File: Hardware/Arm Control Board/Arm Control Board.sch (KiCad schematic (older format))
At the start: 31 parts, among them P1 Servo 1, P10 UIM240XX_Stepper_Conn, P11 Battery, P12 SyRen, P13 Raspberry Pi, P2 Shoulder Feedback, P3 Servo 2, P4 Servo 3, P5 Elbow Feedback, P6 Servo 4, P7 RS485, P8 ST_SWD_Connector, P9 Servo 5, U1 STM32F401RCT6, U2 SN75176BDR, U3 74LVCH244APW, X1 24MHz

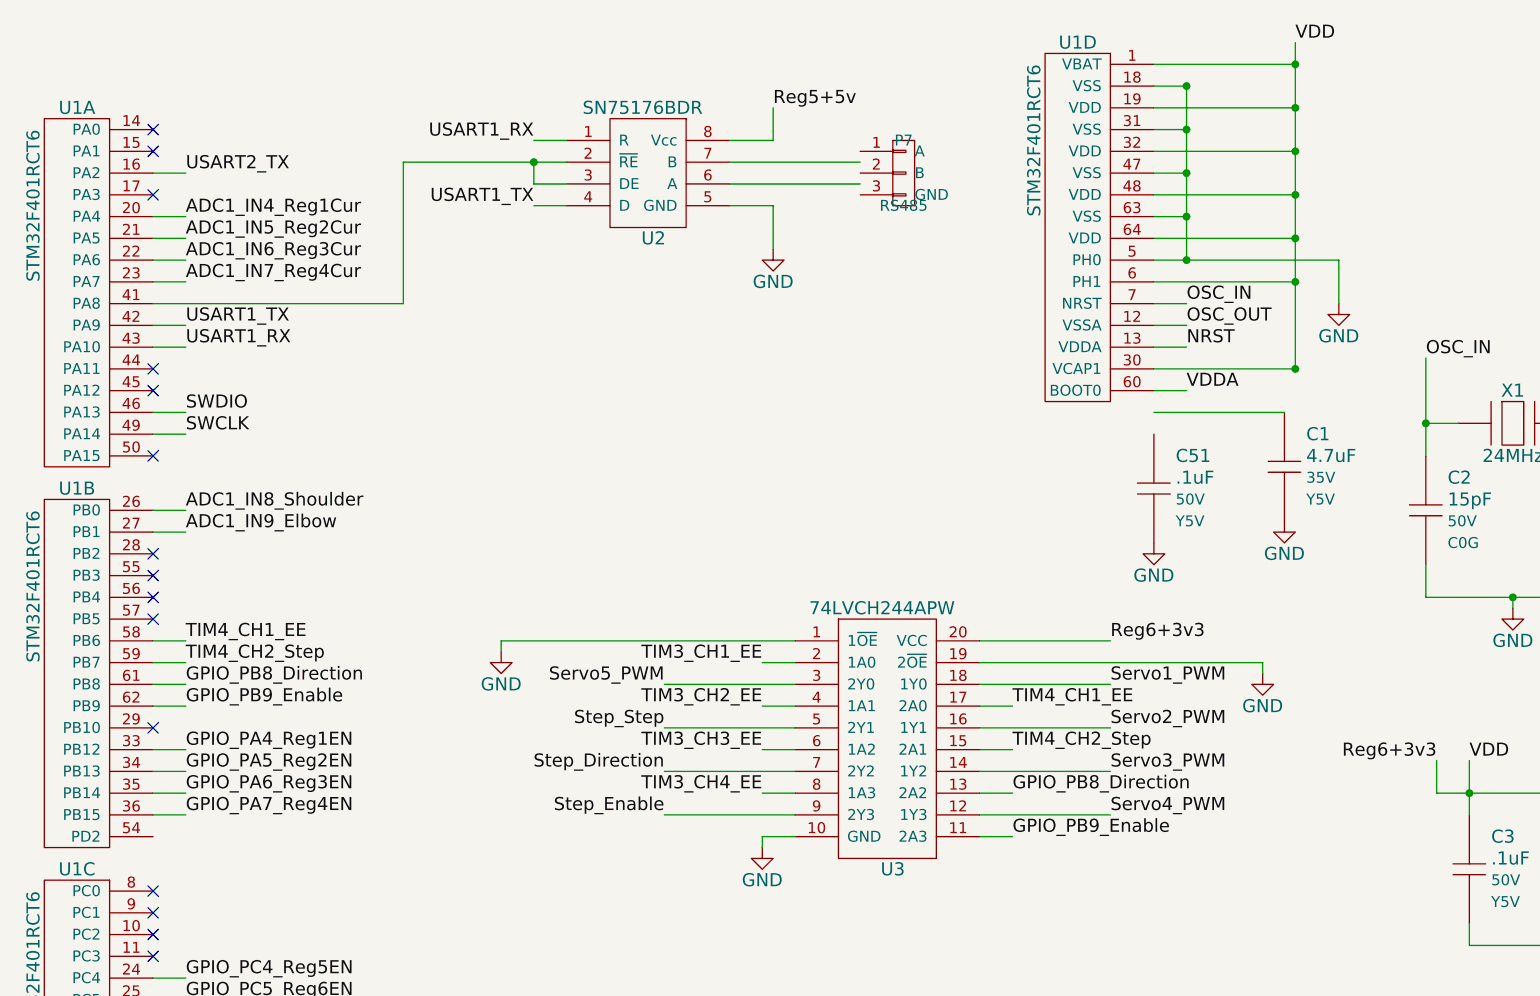
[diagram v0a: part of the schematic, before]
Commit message: Fixed power connections to STM32
The part changes screwed some connections up
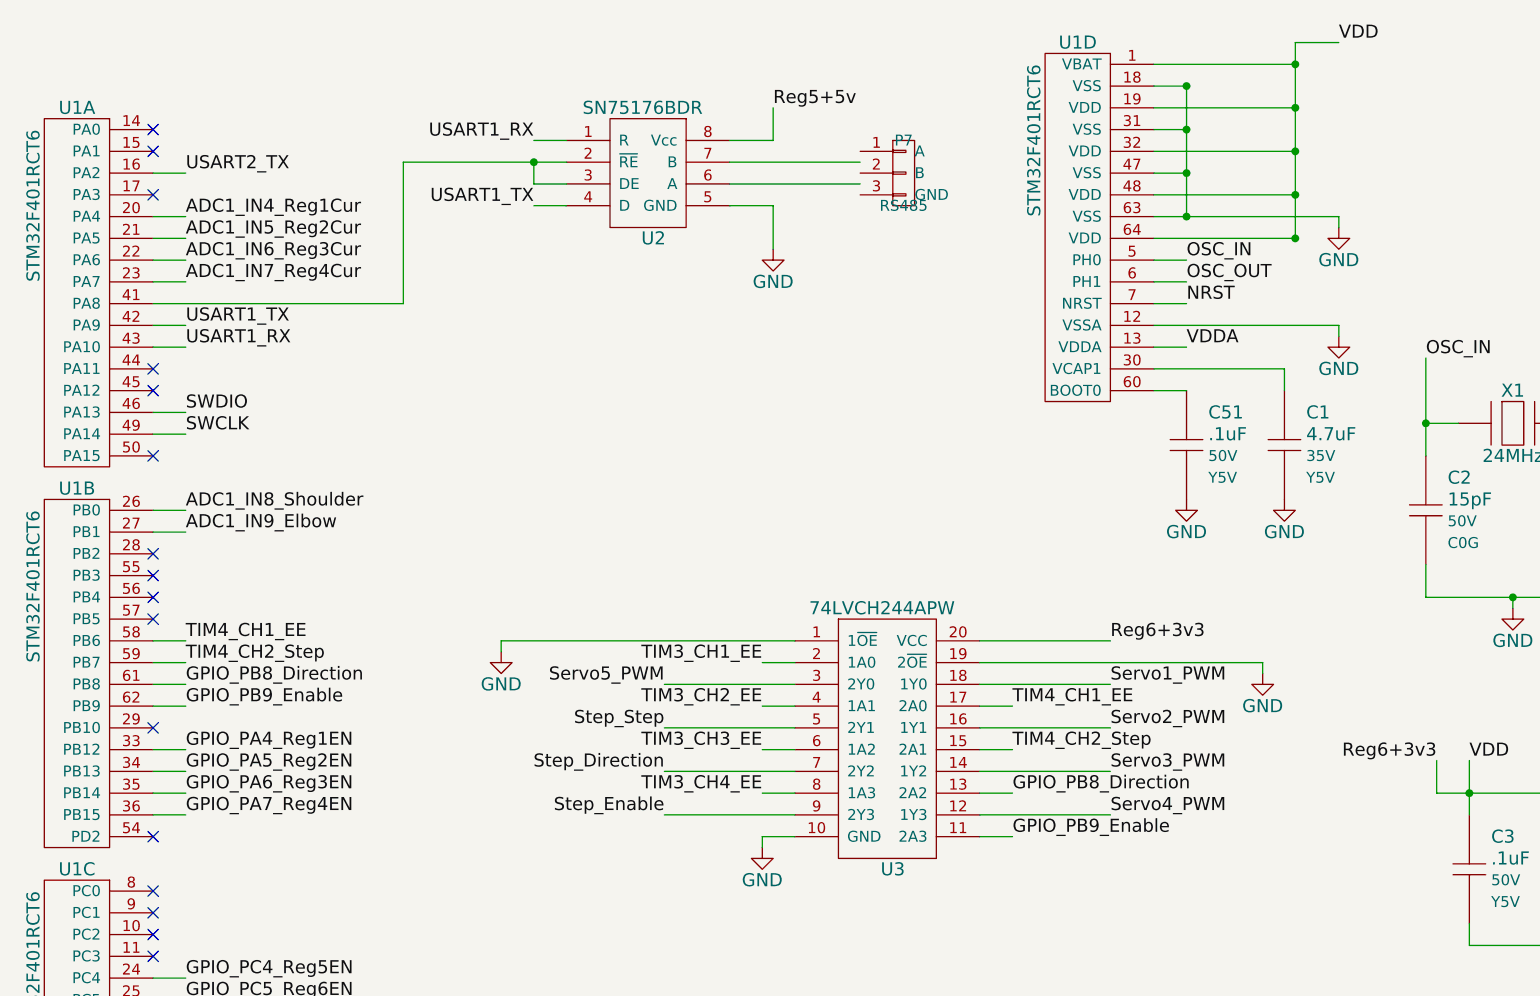
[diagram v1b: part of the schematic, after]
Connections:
- net GND: now also U1.12 (VSSA); no longer U1.5 (PH0)
- net NRST: now also U1.7 (NRST); no longer U1.13 (VDDA)
- net OSC_IN: now also U1.5 (PH0); no longer U1.7 (NRST)
- net OSC_OUT: now also U1.6 (PH1); no longer U1.12 (VSSA)
- net Reg6+3v3: no longer U1.30 (VCAP1), U1.6 (PH1)
- net VDDA: now also U1.13 (VDDA); no longer U1.60 (BOOT0)
- net at C51.1: now also U1.60 (BOOT0)
- net at C1.1: now also U1.30 (VCAP1)
- no-connect marks 22 -> 23
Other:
- moved on the sheet: C1, C51
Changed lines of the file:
@@
 	1    0    0    -1
 $EndComp
-Text Label 6450 650  0    60   ~ 0
+Text Label 6650 650  0    60   ~ 0
 VDD
 $Comp
@@
 Text Label 7250 3950 0    60   ~ 0
 VDD
-Text Label 5950 2250 0    60   ~ 0
+Text Label 5950 2050 0    60   ~ 0
 VDDA
 Text Label 10150 4000 0    60   ~ 0
@@
 Text Label 1350 2450 0    60   ~ 0
 SWCLK
-Text Label 5950 2050 0    60   ~ 0
+Text Label 5950 1850 0    60   ~ 0
 NRST
 $Comp
@@
 L Capacitor C1
 U 1 1 54D0C267
-P 6400 2600
-F 0 "C1" V 6250 2700 60  0000 L CNN
-F 1 "4.7uF" V 6350 2700 60  0000 L CNN
-F 2 "Capacitors_SMD:C_1206_HandSoldering" H 6300 2600 60  0001 C CNN
-F 3 "" H 6400 2700 60  0001 C CNN
-F 4 "Taiyo Yuden" H 6400 2600 60  0001 C CNN "Manufacturer"
-F 5 "GMK316F475ZG-T" H 6400 2600 60  0001 C CNN "Manufacturer Part #"
-F 6 "Digi-Key" H 6400 2600 60  0001 C CNN "Vendor"
-F 7 "587-2254-1-ND" H 6400 2600 60  0001 C CNN "Vendor Part #"
-F 8 "35V" V 6450 2700 50  0000 L CNN "Voltage"
-F 9 "Y5V" V 6550 2700 50  0000 L CNN "Dielectric"
-	1    6400 2600
+P 6400 2500
+F 0 "C1" V 6250 2600 60  0000 L CNN
+F 1 "4.7uF" V 6350 2600 60  0000 L CNN
+F 2 "Capacitors_SMD:C_1206_HandSoldering" H 6300 2500 60  0001 C CNN
+F 3 "" H 6400 2600 60  0001 C CNN
+F 4 "Taiyo Yuden" H 6400 2500 60  0001 C CNN "Manufacturer"
+F 5 "GMK316F475ZG-T" H 6400 2500 60  0001 C CNN "Manufacturer Part #"
+F 6 "Digi-Key" H 6400 2500 60  0001 C CNN "Vendor"
+F 7 "587-2254-1-ND" H 6400 2500 60  0001 C CNN "Vendor Part #"
+F 8 "35V" V 6450 2600 50  0000 L CNN "Voltage"
+F 9 "Y5V" V 6550 2600 50  0000 L CNN "Dielectric"
+	1    6400 2500
 	0    1    1    0
 $EndComp
@@
 L GND #PWR020
 U 1 1 54D0EC2B
-P 6400 2850
-F 0 "#PWR020" H 6400 2600 60  0001 C CNN
-F 1 "GND" H 6400 2700 60  0000 C CNN
-F 2 "" H 6400 2850 60  0000 C CNN
-F 3 "" H 6400 2850 60  0000 C CNN
-	1    6400 2850
-	1    0    0    -1
-$EndComp
-Text Label 5950 1850 0    60   ~ 0
+P 6400 2750
+F 0 "#PWR020" H 6400 2500 60  0001 C CNN
+F 1 "GND" H 6400 2600 60  0000 C CNN
+F 2 "" H 6400 2750 60  0000 C CNN
+F 3 "" H 6400 2750 60  0000 C CNN
+	1    6400 2750
+	1    0    0    -1
+$EndComp
+Text Label 5950 1650 0    60   ~ 0
 OSC_IN
-Text Label 5950 1950 0    60   ~ 0
+Text Label 5950 1750 0    60   ~ 0
 OSC_OUT
 $Comp
@@
 L GND #PWR024
 U 1 1 54CB9E3A
-P 6650 1850
-F 0 "#PWR024" H 6650 1600 60  0001 C CNN
-F 1 "GND" H 6650 1700 60  0000 C CNN
-F 2 "" H 6650 1850 60  0000 C CNN
-F 3 "" H 6650 1850 60  0000 C CNN
-	1    6650 1850
+P 6650 1500
+F 0 "#PWR024" H 6650 1250 60  0001 C CNN
+F 1 "GND" H 6650 1350 60  0000 C CNN
+F 2 "" H 6650 1500 60  0000 C CNN
+F 3 "" H 6650 1500 60  0000 C CNN
+	1    6650 1500
 	1    0    0    -1
 $EndComp
@@
 Wire Wire Line
 	6450 950  5800 950
-Wire Wire Line
-	6450 1750 5800 1750
-Connection ~ 6450 1750
 Wire Wire Line
 	6450 1550 5800 1550
@@
 Wire Wire Line
 	5950 1050 5800 1050
-Wire Wire Line
-	5800 1650 6650 1650
 Connection ~ 5950 1050
 Wire Wire Line
-	5950 1450 5800 1450
+	5800 1450 6650 1450
 Connection ~ 5950 1450
 Wire Wire Line
@@
 Connection ~ 9250 4100
 Wire Wire Line
-	6450 2150 5800 2150
-Connection ~ 6450 2150
-Wire Wire Line
 	9650 4800 9650 4700
 Connection ~ 9650 4800
 Wire Wire Line
-	5800 2250 5950 2250
+	5800 2050 5950 2050
 Wire Wire Line
 	5800 850  5950 850
@@
 	1200 2450 1350 2450
 Wire Wire Line
-	5800 2050 5950 2050
+	5800 1850 5950 1850
 Wire Wire Line
 	5350 6000 5200 6000
@@
 	4050 1100 3850 1100
 Wire Wire Line
-	5800 2350 6400 2350
-Wire Wire Line
-	5800 1850 5950 1850
-Wire Wire Line
-	5800 1950 5950 1950
+	5800 1650 5950 1650
+Wire Wire Line
+	5800 1750 5950 1750
 Wire Wire Line
 	7050 2100 7050 2550
@@
 Connection ~ 8050 5850
 Wire Wire Line
-	5950 850  5950 1650
-Wire Wire Line
-	6650 1650 6650 1850
-Wire Wire Line
-	6450 650  6450 2150
+	6650 1450 6650 1500
 Connection ~ 6450 950
-Connection ~ 5950 1650
 Wire Wire Line
 	5800 750  6450 750
@@
 L Capacitor C51
 U 1 1 54CC6722
-P 5800 2700
-F 0 "C51" V 5650 2800 60  0000 L CNN
-F 1 ".1uF" V 5750 2800 60  0000 L CNN
-F 2 "Capacitors_SMD:C_1206_HandSoldering" H 5700 2700 60  0001 C CNN
-F 3 "" H 5800 2800 60  0001 C CNN
-F 4 "Samsung Electro-Mechanics" H 5800 2700 60  0001 C CNN "Manufacturer"
-F 5 "CL31F104MBCNNNC" H 5800 2700 60  0001 C CNN "Manufacturer Part #"
-F 6 "Digi-Key" H 5800 2700 60  0001 C CNN "Vendor"
-F 7 "1276-2854-1-ND" H 5800 2700 60  0001 C CNN "Vendor Part #"
-F 8 "50V" V 5850 2800 50  0000 L CNN "Voltage"
-F 9 "Y5V" V 5950 2800 50  0000 L CNN "Dielectric"
-	1    5800 2700
+P 5950 2500
+F 0 "C51" V 5800 2600 60  0000 L CNN
+F 1 ".1uF" V 5900 2600 60  0000 L CNN
+F 2 "Capacitors_SMD:C_1206_HandSoldering" H 5850 2500 60  0001 C CNN
+F 3 "" H 5950 2600 60  0001 C CNN
+F 4 "Samsung Electro-Mechanics" H 5950 2500 60  0001 C CNN "Manufacturer"
+F 5 "CL31F104MBCNNNC" H 5950 2500 60  0001 C CNN "Manufacturer Part #"
+F 6 "Digi-Key" H 5950 2500 60  0001 C CNN "Vendor"
+F 7 "1276-2854-1-ND" H 5950 2500 60  0001 C CNN "Vendor Part #"
+F 8 "50V" V 6000 2600 50  0000 L CNN "Voltage"
+F 9 "Y5V" V 6100 2600 50  0000 L CNN "Dielectric"
+	1    5950 2500
 	0    1    1    0
 $EndComp
@@
 L GND #PWR025
 U 1 1 54CC691C
-P 5800 2950
-F 0 "#PWR025" H 5800 2700 60  0001 C CNN
-F 1 "GND" H 5800 2800 60  0000 C CNN
-F 2 "" H 5800 2950 60  0000 C CNN
-F 3 "" H 5800 2950 60  0000 C CNN
-	1    5800 2950
+P 5950 2750
+F 0 "#PWR025" H 5950 2500 60  0001 C CNN
+F 1 "GND" H 5950 2600 60  0000 C CNN
+F 2 "" H 5950 2750 60  0000 C CNN
+F 3 "" H 5950 2750 60  0000 C CNN
+	1    5950 2750
 	1    0    0    -1
 $EndComp
@@
 Text Label 9300 2050 2    60   ~ 0
 ADC1_IN7_Reg4Cur
+NoConn ~ 1200 4300
+Wire Wire Line
+	5950 850  5950 1450
+Wire Wire Line
+	6450 650  6450 1550
+Wire Wire Line
+	5800 2250 5950 2250
+Wire Wire Line
+	5800 2150 6400 2150
+Wire Wire Line
+	6400 2150 6400 2250
+Wire Wire Line
+	6450 650  6650 650
+Wire Wire Line
+	5800 1950 6650 1950
+Wire Wire Line
+	6650 1950 6650 2000
+$Comp
+L GND #PWR?
+U 1 1 54D8F98A
+P 6650 2000
+F 0 "#PWR?" H 6650 1750 60  0001 C CNN
+F 1 "GND" H 6650 1850 60  0000 C CNN
+F 2 "" H 6650 2000 60  0000 C CNN
+F 3 "" H 6650 2000 60  0000 C CNN
+	1    6650 2000
+	1    0    0    -1
+$EndComp
 $EndSCHEMATC

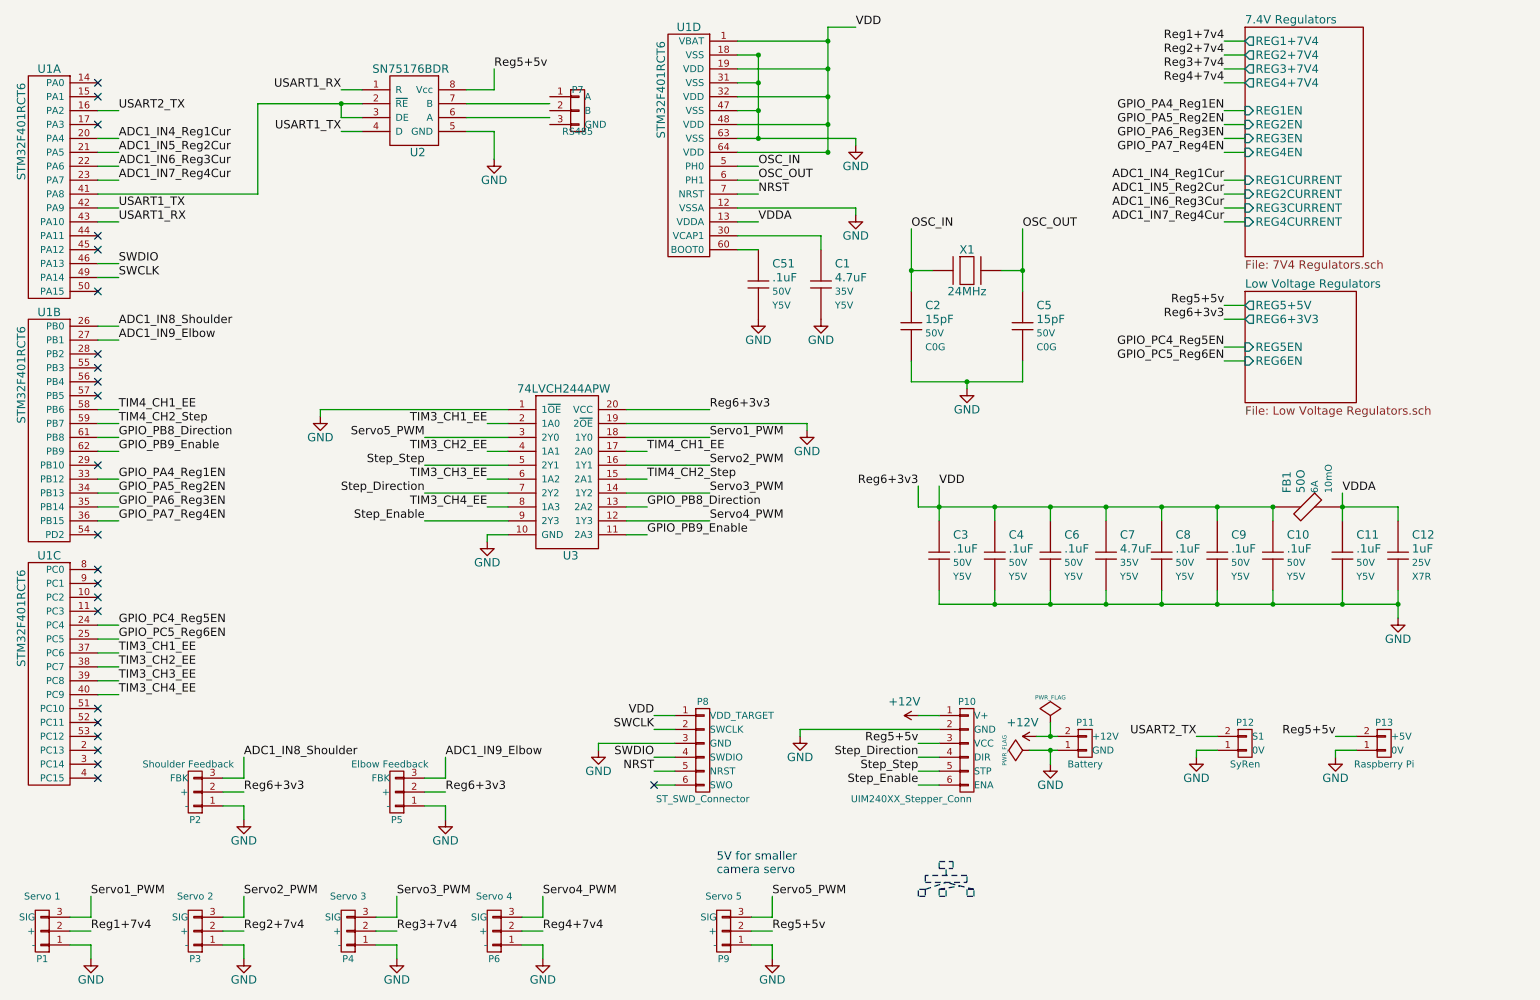
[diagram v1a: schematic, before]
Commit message: Added clamp force sensor port in cube and schematic
Resolves #20
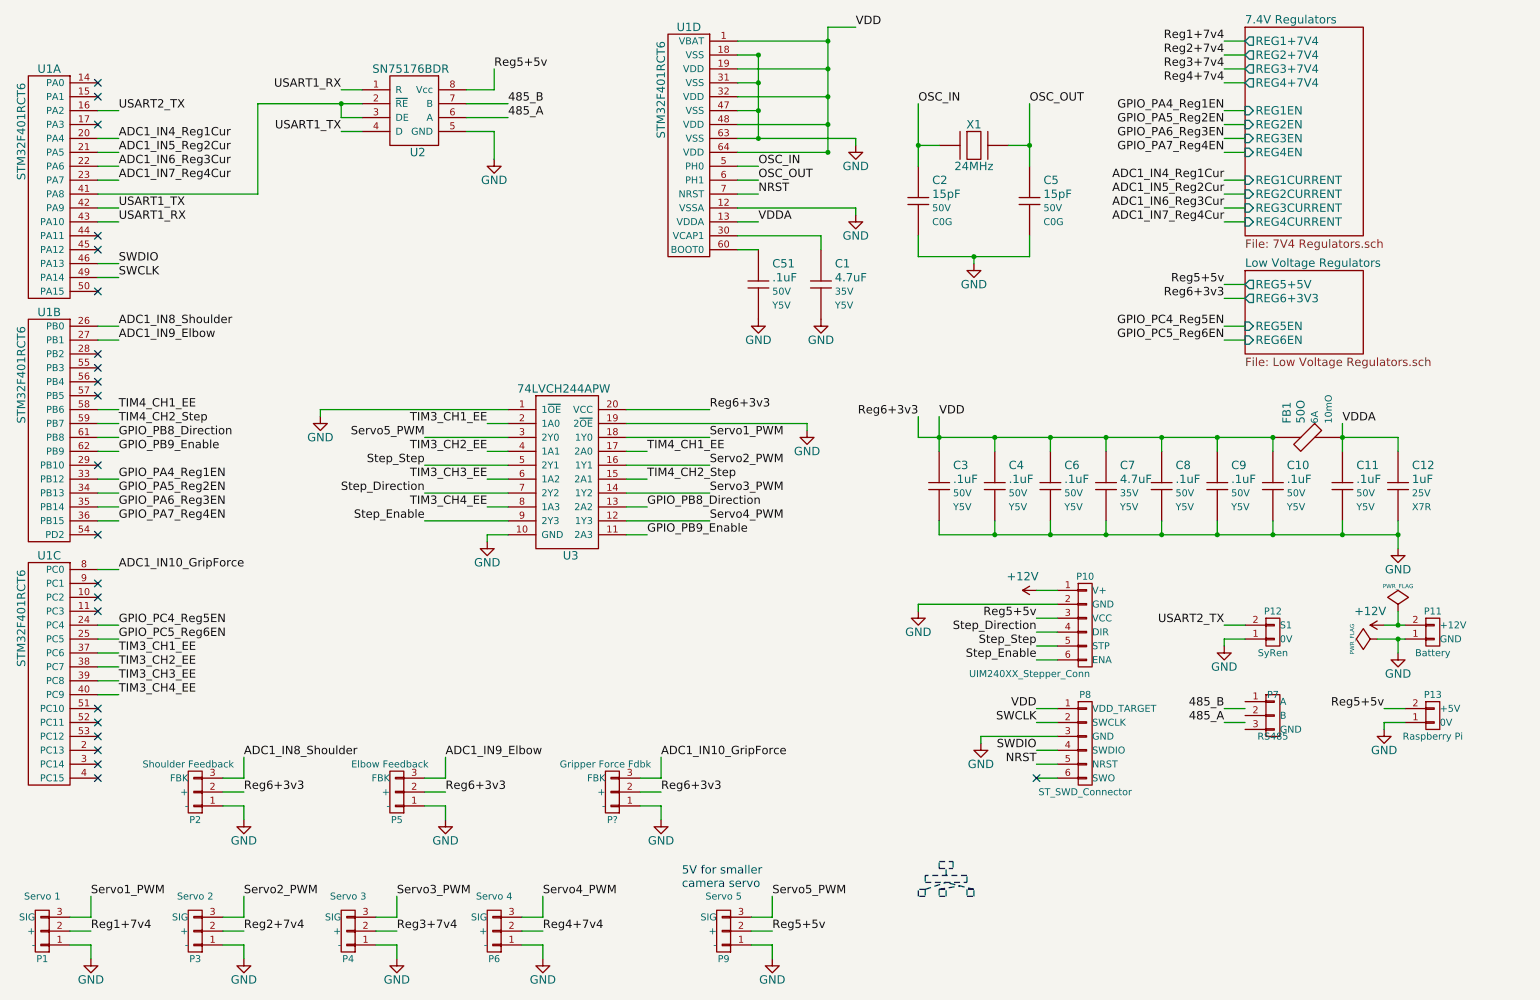
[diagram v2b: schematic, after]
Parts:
- added P?: Gripper Force Fdbk, MAVRIC_footprints:1x3_SMD_header, symbol Actuator_Pot
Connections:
- net GND: now also P?.1 (-)
- net Reg6+3v3: now also P?.2 (+)
- net 485_A: now reaches U2.6 (A)
- net 485_B: now reaches U2.7 (B)
- net ADC1_IN10_GripForce: now reaches U1.8 (PC0)
- net ADC1_IN10_GripForce: now also P?.3 (FBK)
- no-connect marks 23 -> 22
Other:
- moved on the sheet: C10, C11, C12, C2, C3, C4, C5, C6, C7, C8, C9, FB1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

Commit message: Lay out regulators 1-4, update cube for oscillator
Got strangely excited about this commit. Almost called my dad...
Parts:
- gave numbers to parts that had none: 1
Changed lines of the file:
@@
 	6650 1950 6650 2000
 $Comp
-L GND #PWR?
+L GND #PWR026
 U 1 1 54D8F98A
 P 6650 2000
-F 0 "#PWR?" H 6650 1750 60  0001 C CNN
+F 0 "#PWR026" H 6650 1750 60  0001 C CNN
 F 1 "GND" H 6650 1850 60  0000 C CNN
 F 2 "" H 6650 2000 60  0000 C CNN
@@
 485_A
 $Comp
-L Actuator_Pot P?
+L Actuator_Pot P14
 U 1 1 54DB2297
 P 4900 6150
-F 0 "P?" H 4900 6350 50  0000 C CNN
+F 0 "P14" H 4900 6350 50  0000 C CNN
 F 1 "Gripper Force Fdbk" H 4950 5950 50  0000 C CNN
 F 2 "MAVRIC_footprints:1x3_SMD_header" H 4900 6150 60  0001 C CNN
@@
 $EndComp
 $Comp
-L GND #PWR?
+L GND #PWR027
 U 1 1 54DB229D
 P 5250 6350
-F 0 "#PWR?" H 5250 6100 60  0001 C CNN
+F 0 "#PWR027" H 5250 6100 60  0001 C CNN
 F 1 "GND" H 5250 6200 60  0000 C CNN
 F 2 "" H 5250 6350 60  0000 C CNN
